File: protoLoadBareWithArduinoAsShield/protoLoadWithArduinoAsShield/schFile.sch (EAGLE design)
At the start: 11 parts, among them IC1 QUAD_OPAMPP, X1 4 Screw Terminal

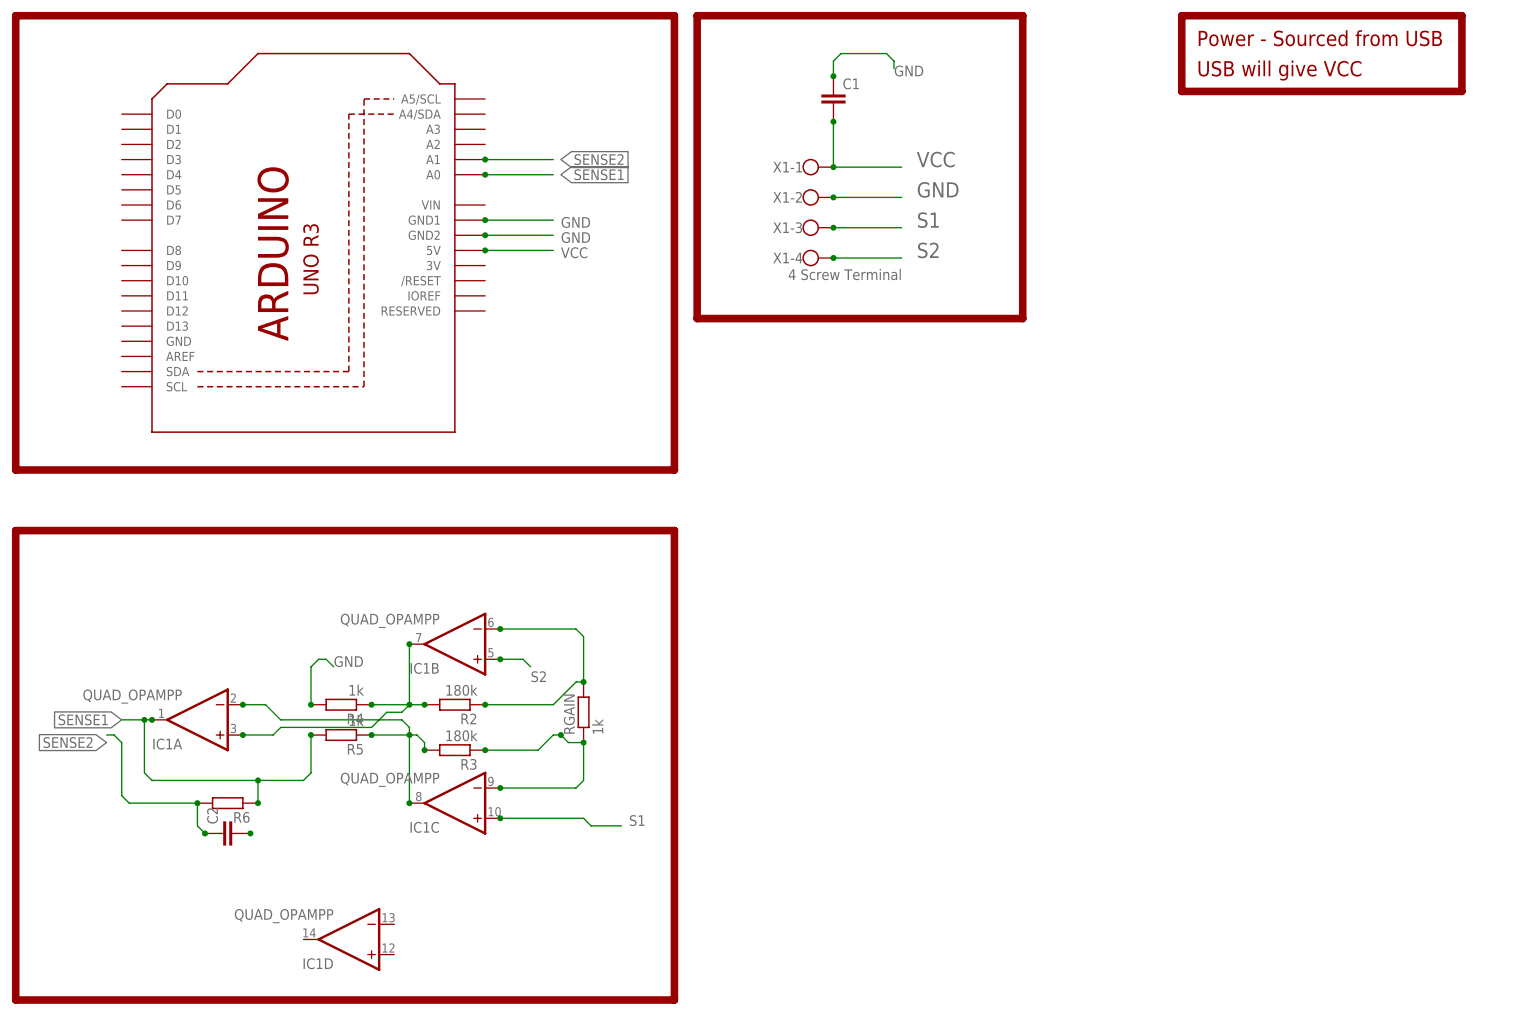
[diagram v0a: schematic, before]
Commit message: added schematic nd board file, shield, for reference.
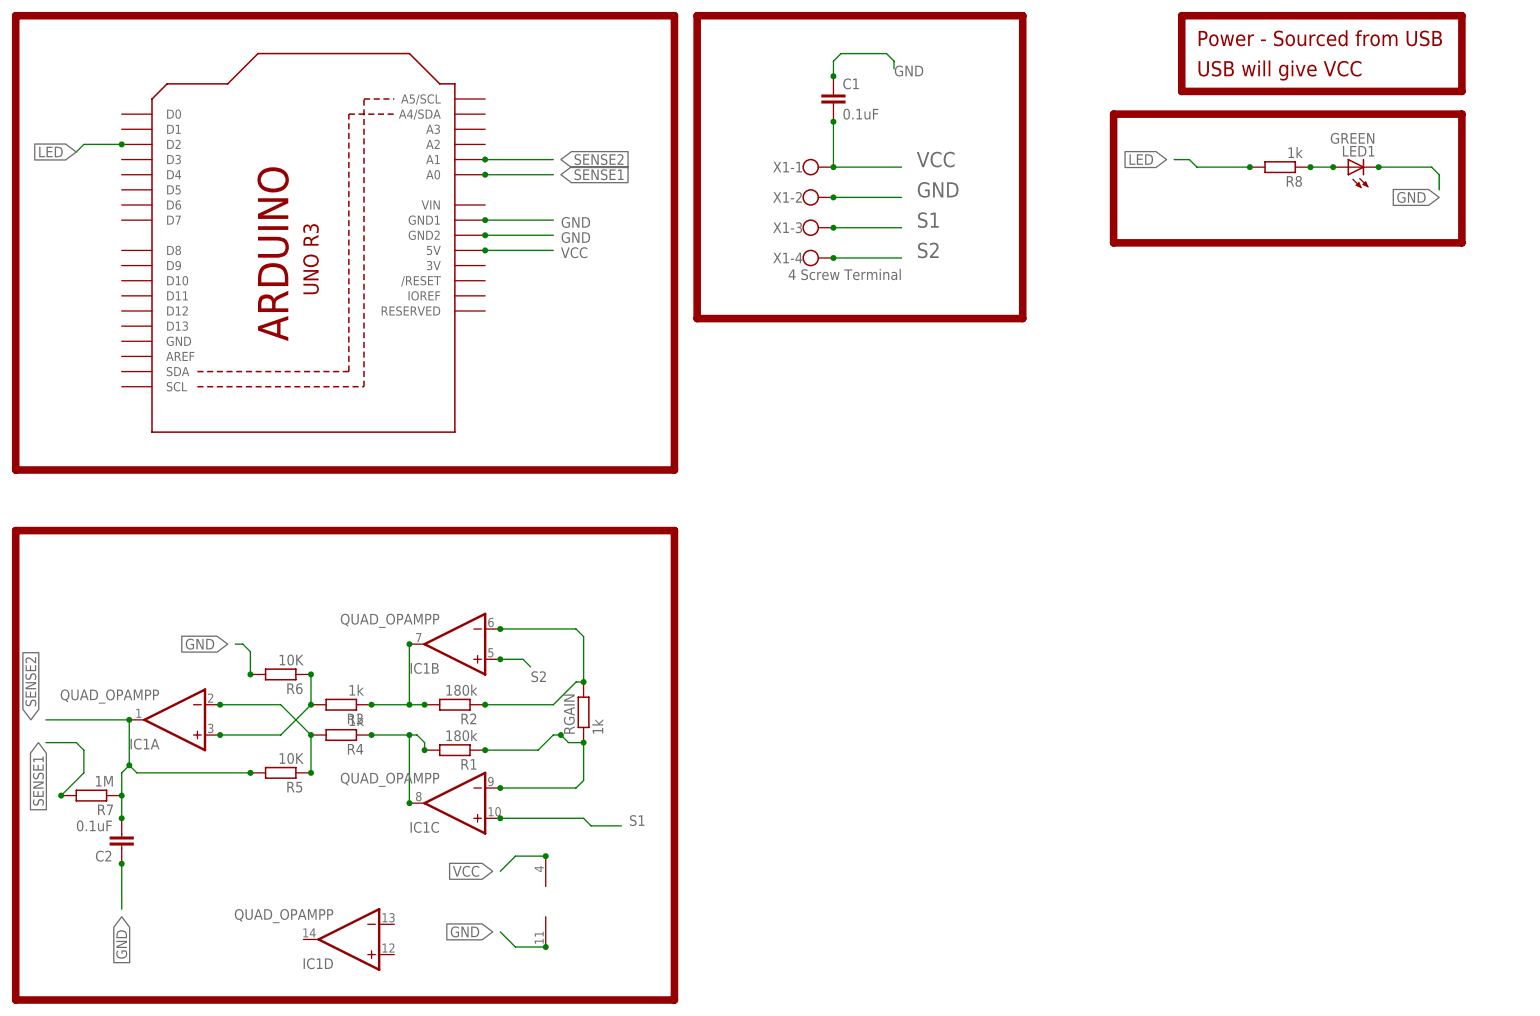
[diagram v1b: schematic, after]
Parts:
- added LED1: GREEN, adafruit:LED3MM
- added R1: 180k, resistor:R-EU_0207/10
- added R7: 1M, resistor:R-EU_0207/10
- added R8: 1k, resistor:R-EU_0207/10
- C1, C2: value (none) -> 0.1uF
- R3: value 180k -> 1k
- R5: value 1k -> 10K
- R6: value (none) -> 10K
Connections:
- removed net N$2: IC1A.-IN, IC1C.OUT, R3.2, R5.1
- removed net N$8: C2.2
- new net LED: ARDUINO.D2, R8.2
- new net N$13: IC1C.OUT, R1.2, R4.1
- new net N$3: IC1A.-IN, R4.2, R5.1
- new net N$5: LED1.A, R8.1
- new net N$6: IC1A.+IN, R3.2, R6.1
- net GND: now also C2.1, IC1P.V-, LED1.C, R6.2; no longer R4.2
- net N$1: now also R3.1; no longer IC1A.+IN, R4.1
- net N$4: now also R1.1; no longer R3.1
- net SENSE1: now also R7.2; no longer IC1A.OUT, R5.2, R6.1
- net SENSE2: now also C2.2, IC1A.OUT, R5.2, R7.1; no longer C2.1, R6.2
- net VCC: now also IC1P.V+
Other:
- moved on the sheet: C2, IC1A, R3, R4, R5, R6
